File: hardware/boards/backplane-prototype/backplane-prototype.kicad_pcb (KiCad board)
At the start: 4 copper layers, 151.8 x 30.8 mm, 93 parts, among them J1 SLOT_1, J10 SWD, J11 12V 3-WIRE FAN, J12 DS18B20 EXT SUPPLY, J2 XY308-2.54-3P / EXTERNAL CAN, J3 SLOT_2, J4 SLOT_3, J5 DC IN, J6 SLOT_4, J7 SLOT_5, J8 SLOT_6, J9 12V 3-WIRE FAN, Q1 AO3407A, Q2 2N7002, Q3 AO3407A, Q4 2N7002, U1 STM32C092GCU6, U2 LM5164DDAR, U3 LM5164DDAR, U4 INA237AIDGSR, U5 TCAN3413DR

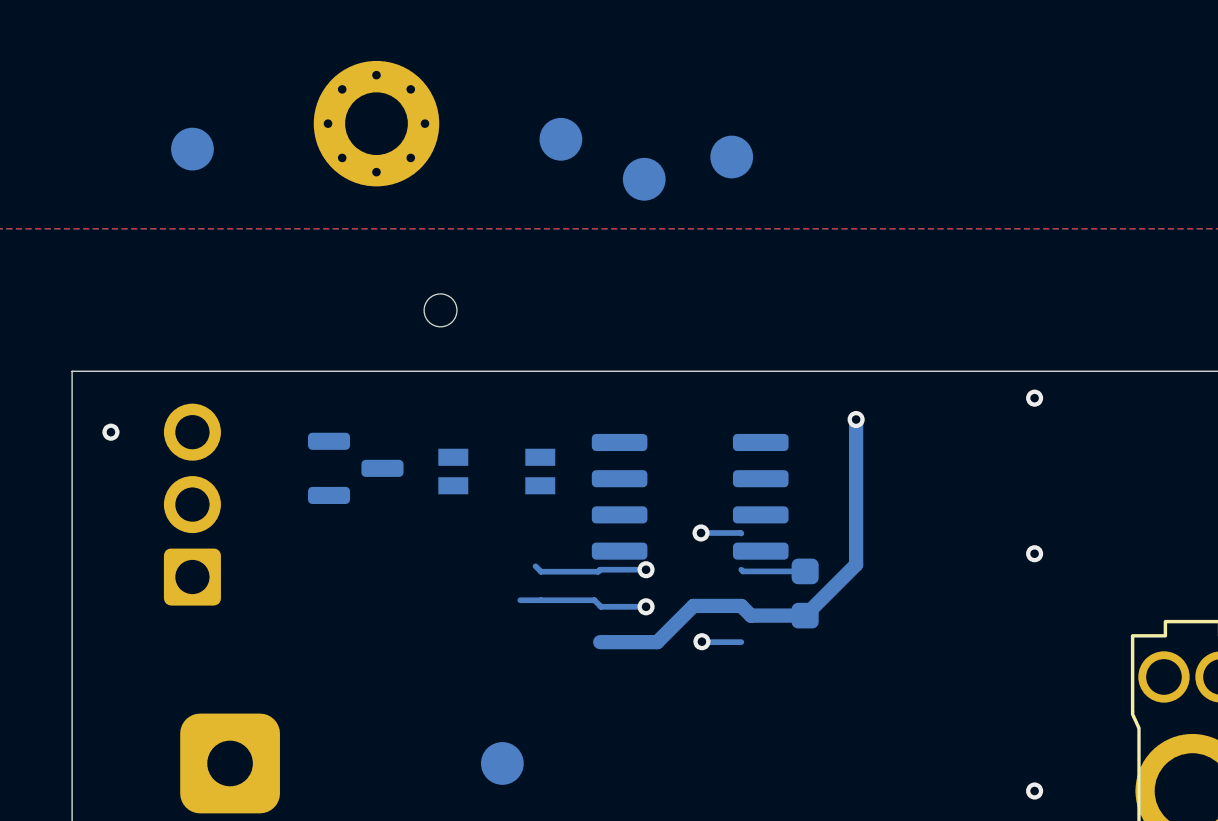
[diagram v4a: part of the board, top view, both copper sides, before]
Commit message: checkpoint: save CAN schematic and layout updates
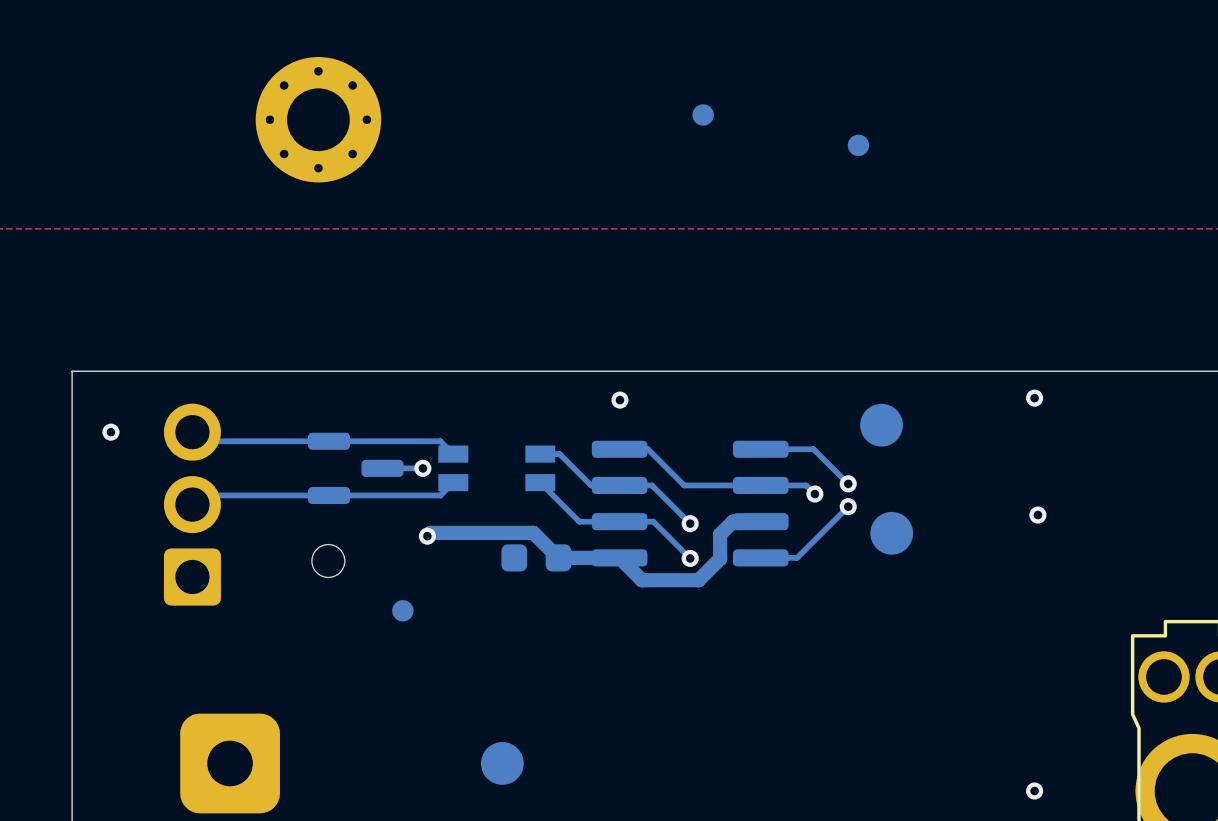
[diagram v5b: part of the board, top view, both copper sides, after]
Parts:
- removed TP15: CAN_BUS_P, TestPoint:TestPoint_Pad_D1.5mm
- removed TP16: CAN_BUS_N, TestPoint:TestPoint_Pad_D1.5mm
- added REF**: Fiducial_0.75mm_Mask1.5mm, Fiducial:Fiducial_0.75mm_Mask1.5mm, B.Cu at (41.1, 55.1)
- added REF**: Fiducial_0.75mm_Mask1.5mm, Fiducial:Fiducial_0.75mm_Mask1.5mm, B.Cu at (51.6, 37.7)
- added REF**: Fiducial_0.75mm_Mask1.5mm, Fiducial:Fiducial_0.75mm_Mask1.5mm, B.Cu at (57.1, 38.8)
- moved TP7 15.1 mm to (58.2, 52.4)
- moved TP6 10.8 mm to (57.9, 48.6)
- moved H9 9.63 mm to (38.5, 53.4)
- moved C20 9.51 mm to (45.8, 53.2), turned to 180 degrees
- moved H1 2.04 mm to (38.1, 37.9)
- moved U5 0.24 mm to (51.2, 51.3)
- moved L3 0.11 mm to (44.4, 50.1)
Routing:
- net /CAN-FD and Six Slots/CAN_EXT_N: track 0.00 -> 9.47 mm
- net /CAN-FD and Six Slots/CAN_EXT_P: track 0.13 -> 9.60 mm
- net GND: track 41.0 -> 47.6 mm, vias 58 -> 61
- net CAN_RX: track 106.3 -> 99.9 mm
- net CAN_TX: track 103.4 -> 99.7 mm
- net +3V3: track 274.8 -> 273.1 mm
- net /CAN-FD and Six Slots/CAN_BUS_P: track 140.1 -> 139.3 mm

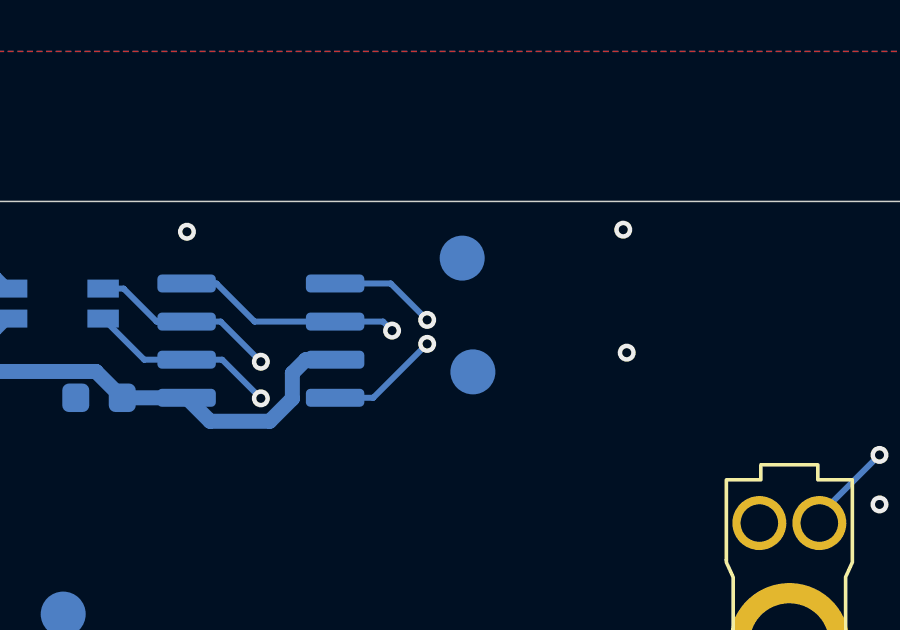
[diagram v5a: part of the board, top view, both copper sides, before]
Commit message: Move CAN test points beside signal vias
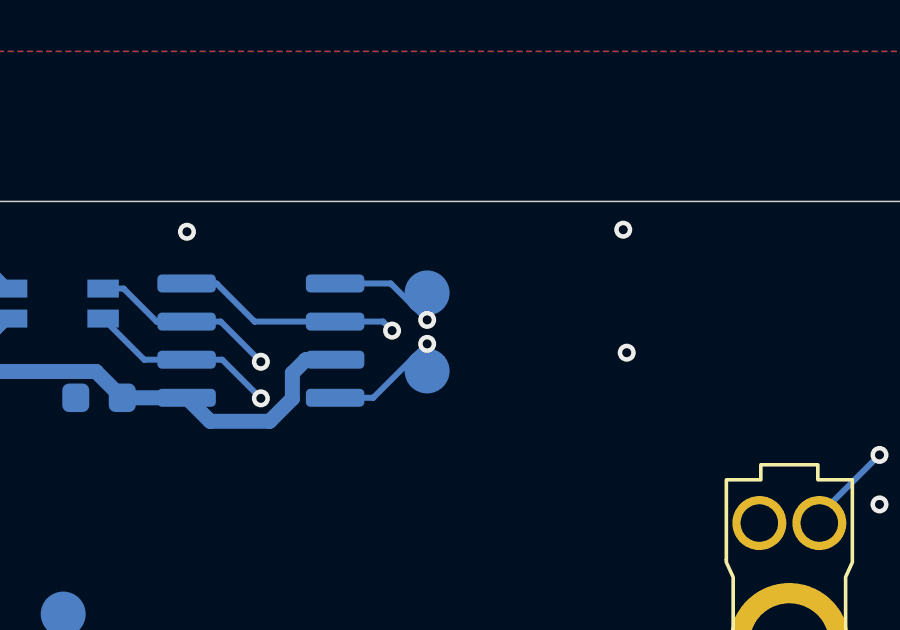
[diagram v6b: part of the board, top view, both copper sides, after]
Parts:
- moved TP6 1.65 mm to (56.7, 49.8)
- moved TP7 1.53 mm to (56.7, 52.4)
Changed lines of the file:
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@@
 	(footprint "TestPoint:TestPoint_Pad_D1.5mm"
 		(layer "B.Cu")
-		(at 57.889587 48.589479 180)
+		(at 56.72 49.75 180)
 		(descr "SMD pad as test Point, diameter 1.5mm")
 		(tags "test point SMD pad")
 		(property "Reference" "TP6"
-			(at 0 1.648 0)
+			(at -1.75 0 90)
 			(layer "B.SilkS")
 			(effects
@@
 			(end 0 -0.95)
 			(stroke
-				(width 0.12)
+				(width 0.15)
 				(type solid)
 			)
@@
 	(footprint "TestPoint:TestPoint_Pad_D1.5mm"
 		(layer "B.Cu")
-		(at 58.246097 52.381446 180)
+		(at 56.72 52.35 180)
 		(descr "SMD pad as test Point, diameter 1.5mm")
 		(tags "test point SMD pad")
 		(property "Reference" "TP7"
-			(at 0 1.648 0)
+			(at -3.28 0 90)
 			(layer "B.SilkS")
 			(effects
@@
 			(end 0 -0.95)
 			(stroke
-				(width 0.12)
-				(type solid)
-			)
+				(width 0.15)
+				(type solid)
+			)

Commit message: checkpoint: save current backplane layout
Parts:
- moved H9 14.7 mm to (50.5, 44.9)
- moved C20 14.7 mm to (57.8, 44.8)
- moved D1 14.7 mm to (51.4, 41.7)
- moved L3 14.7 mm to (56.4, 41.7)
- moved TP6 14.7 mm to (68.7, 41.3)
- moved TP7 14.7 mm to (68.7, 43.9)
- moved U5 14.7 mm to (63.2, 42.9)
- moved REF** 13.2 mm to (39.6, 42.0)
- moved H1 12.3 mm to (39.9, 50.1)
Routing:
- net /CAN-FD and Six Slots/CAN_EXT_N: track 9.47 -> 5.00 mm
- net /CAN-FD and Six Slots/CAN_EXT_P: track 9.60 -> 5.13 mm
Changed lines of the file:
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@@
 	(footprint "mini-rack-power:MountingHole_2.2mm_M2_Pad_Via_JLC"
 		(layer "F.Cu")
-		(at 38.138968 37.877687)
+		(at 39.863604 50.091978)
 		(descr "Mounting Hole 2.2mm, M2, with 0.3 mm stitching drills, 0.26 mm annular rings, and 0.45 mm hole clearance")
 		(tags "mountinghole M2 JLCPCB")
@@
 	(footprint "Capacitor_SMD:C_0603_1608Metric"
 		(layer "B.Cu")
-		(at 45.783704 53.245 180)
+		(at 57.775494 44.819757 180)
 		(descr "Capacitor SMD 0603 (1608 Metric), square (rectangular) end terminal, IPC-7351 nominal, (Body size source: IPC-SM-782 page 76, https://www.pcb-3d.com/wordpress/wp-content/uploads/ipc-sm-782a_amendment_1_and_2.pdf)")
 		(tags "capacitor")
@@
 	(footprint "Fiducial:Fiducial_0.75mm_Mask1.5mm"
 		(layer "B.Cu")
-		(at 41.101509 55.100021 180)
+		(at 39.641394 41.981327 180)
 		(descr "Fiducial, circular marking, 0.75mm bare copper, 1.5mm soldermask opening (Level B)")
 		(tags "fiducial")
@@
 	(footprint "TestPoint:TestPoint_Pad_D1.5mm"
 		(layer "B.Cu")
-		(at 56.72 49.75 180)
+		(at 68.71179 41.324757 180)
 		(descr "SMD pad as test Point, diameter 1.5mm")
 		(tags "test point SMD pad")
@@
 	(footprint "TestPoint:TestPoint_Pad_D1.5mm"
 		(layer "B.Cu")
-		(at 56.72 52.35 180)
+		(at 68.71179 43.924757 180)
 		(descr "SMD pad as test Point, diameter 1.5mm")
 		(tags "test point SMD pad")
@@
 	(footprint "mini-rack-power:MountingHole_JLCPCB_Tooling_1.152mm"
 		(layer "B.Cu")
-		(at 38.486819 53.353745 180)
+		(at 50.478609 44.928502 180)
 		(descr "JLCPCB PCBA tooling hole: 1.152 mm round NPTH with 0.148 mm solder-mask expansion")
 		(tags "mountinghole tooling JLCPCB PCBA NPTH 1.152mm")
@@
 	(footprint "Package_SO:SOIC-8_3.9x4.9mm_P1.27mm"
 		(layer "B.Cu")
-		(at 51.17833 51.34 180)
+		(at 63.17012 42.914757 180)
 		(descr "SOIC, 8 Pin (JEDEC MS-012AA, https://www.analog.com/media/en/package-pcb-resources/package/pkg_pdf/soic_narrow-r/r_8.pdf)")
 		(tags "SOIC SO")
@@
 	)
 	(footprint "mini-rack-power:L_CommonModeChoke_TDK_ACT1210D"
-		(locked yes)
 		(layer "B.Cu")
-		(at 44.394686 50.105 180)
+		(at 56.386476 41.679757 180)
 		(descr "TDK ACT1210D automotive CAN/CAN-FD common-mode choke, 3.2 x 2.5 mm body; manufacturer recommended 4.1 x 1.6 mm land pattern")
 		(tags "common mode choke CAN CAN-FD TDK ACT1210D C3039743")
@@
 	)
 	(footprint "Package_TO_SOT_SMD:SOT-23"
-		(locked yes)
 		(layer "B.Cu")
-		(at 39.447877 50.105)
+		(at 51.439667 41.679757)
 		(descr "SOT, 3 Pin (JEDEC TO-236 Var AB https://www.jedec.org/document_search?search_api_views_fulltext=TO-236)")
 		(tags "SOT TO_SOT_SMD")
@@
 	)
 	(footprint "mini-rack-power:TerminalBlock_Xinya_XY308-2.54-3P_1x03_P2.54mm_Horizontal"
+		(locked yes)
 		(layer "B.Cu")
 		(at 33.72 53.915 90)
@@
 	)
 	(via
-		(at 48.715082 47.710566)
+		(at 60.706872 39.285323)
 		(size 0.6)
 		(drill 0.3)
@@
 	)
 	(via
-		(at 55.552012 51.005603)
+		(at 67.543802 42.58036)
 		(size 0.6)
 		(drill 0.3)
@@
 	)
 	(via
-		(at 41.803281 50.105)
+		(at 53.795071 41.679757)
 		(size 0.6)
 		(drill 0.3)
@@
 	)
 	(segment
-		(start 50.969756 50.705)
-		(end 49.699756 49.435)
+		(start 62.961546 42.279757)
+		(end 61.691546 41.009757)
 		(width 0.2)
 		(layer "B.Cu")
@@
 	)
 	(segment
-		(start 53.65333 50.705)
-		(end 50.969756 50.705)
+		(start 65.64512 42.279757)
+		(end 62.961546 42.279757)
 		(width 0.2)
 		(layer "B.Cu")
@@
 	)
 	(segment
-		(start 49.699756 49.435)
-		(end 48.70333 49.435)
+		(start 61.691546 41.009757)
+		(end 60.69512 41.009757)
 		(width 0.2)
 		(layer "B.Cu")
@@
 	)
 	(segment
-		(start 55.552012 51.005603)
-		(end 55.251409 50.705)
+		(start 67.543802 42.58036)
+		(end 67.243199 42.279757)
 		(width 0.2)
 		(layer "B.Cu")
@@
 	)
 	(segment
-		(start 41.803281 50.105)
-		(end 40.385377 50.105)
+		(start 53.795071 41.679757)
+		(end 52.377167 41.679757)
 		(width 0.2)
 		(layer "B.Cu")
@@
 	)
 	(segment
-		(start 55.251409 50.705)
-		(end 53.65333 50.705)
+		(start 67.243199 42.279757)
+		(end 65.64512 42.279757)
 		(width 0.2)
 		(layer "B.Cu")
@@
 	)
 	(via
-		(at 51.17833 52.043935)
+		(at 63.17012 43.618692)
 		(size 0.6)
 		(drill 0.3)
 		(layers "F.Cu" "B.Cu")
-		(locked yes)
 		(net "/CAN-FD and Six Slots/CAN_BUS_P")
 	)
@@
 	)
 	(segment
-		(start 48.70333 50.705)
-		(end 47.70333 50.705)
+		(start 60.69512 42.279757)
+		(end 59.69512 42.279757)
 		(width 0.2)
 		(layer "B.Cu")
@@
 	)
 	(segment
-		(start 47.70333 50.705)
-		(end 46.60333 49.605)
+		(start 59.69512 42.279757)
+		(end 58.59512 41.179757)
 		(width 0.2)
 		(layer "B.Cu")
@@
 	)
 	(segment
-		(start 51.17833 52.043935)
-		(end 49.839395 50.705)
+		(start 63.17012 43.618692)
+		(end 61.831185 42.279757)
 		(width 0.2)
 		(layer "B.Cu")
@@
 	)
 	(segment
-		(start 49.839395 50.705)
-		(end 48.70333 50.705)
+		(start 61.831185 42.279757)
+		(end 60.69512 42.279757)
 		(width 0.2)
 		(layer "B.Cu")
@@
 	)
 	(segment
-		(start 46.60333 49.605)
-		(end 45.919686 49.605)
+		(start 58.59512 41.179757)
+		(end 57.911476 41.179757)
 		(width 0.2)
 		(layer "B.Cu")
@@
 	)
 	(via
-		(at 51.17833 53.263576)
+		(at 63.17012 44.838333)
 		(size 0.6)
 		(drill 0.3)
 		(layers "F.Cu" "B.Cu")
-		(locked yes)
 		(net "/CAN-FD and Six Slots/CAN_BUS_N")
 	)
@@
 	)
 	(segment
-		(start 47.289686 51.975)
-		(end 45.919686 50.605)
+		(start 59.281476 43.549757)
+		(end 57.911476 42.179757)
 		(width 0.2)
 		(layer "B.Cu")
@@
 	)
 	(segment
-		(start 48.70333 51.975)
-		(end 47.289686 51.975)
+		(start 60.69512 43.549757)
+		(end 59.281476 43.549757)
 		(width 0.2)
 		(layer "B.Cu")
@@
 	)
 	(segment
-		(start 51.17833 53.263576)
-		(end 49.889754 51.975)
+		(start 63.17012 44.838333)
+		(end 61.881544 43.549757)
 		(width 0.2)
 		(layer "B.Cu")
@@
 	)
 	(segment
-		(start 49.889754 51.975)
-		(end 48.70333 51.975)
+		(start 61.881544 43.549757)
+		(end 60.69512 43.549757)
 		(width 0.2)
 		(layer "B.Cu")
@@
 	)
 	(via
-		(at 41.961545 52.482437)
+		(at 53.953335 44.057194)
 		(size 0.6)
 		(drill 0.3)
@@
 	)
 	(segment
-		(start 51.474633 54.027934)
-		(end 52.22833 53.274237)
+		(start 63.466423 45.602691)
+		(end 64.22012 44.848994)
 		(width 0.5)
 		(layer "B.Cu")
@@
 	)
 	(segment
-		(start 52.22833 52.425001)
-		(end 52.678331 51.975)
+		(start 64.22012 43.999758)
+		(end 64.670121 43.549757)
 		(width 0.5)
 		(layer "B.Cu")
@@
 	)
 	(segment
-		(start 41.961545 52.482437)
-		(end 42.076038 52.367944)
+		(start 53.953335 44.057194)
+		(end 54.067828 43.942701)
 		(width 0.5)
 		(layer "B.Cu")
@@
 	)
 	(segment
-		(start 49.486264 54.027934)
-		(end 48.70333 53.245)
+		(start 61.478054 45.602691)
+		(end 60.69512 44.819757)
 		(width 0.5)
 		(layer "B.Cu")
@@
 	)
 	(segment
-		(start 51.474633 54.027934)
-		(end 49.486264 54.027934)
+		(start 63.466423 45.602691)
+		(end 61.478054 45.602691)
 		(width 0.5)
 		(layer "B.Cu")
@@
 	)
 	(segment
-		(start 42.076038 52.367944)
-		(end 45.681648 52.367944)
+		(start 54.067828 43.942701)
+		(end 57.673438 43.942701)
 		(width 0.5)
 		(layer "B.Cu")
@@
 	)
 	(segment
-		(start 52.678331 51.975)
-		(end 53.65333 51.975)
+		(start 64.670121 43.549757)
+		(end 65.64512 43.549757)
 		(width 0.5)
 		(layer "B.Cu")
@@
 	)
 	(segment
-		(start 45.681648 52.367944)
-		(end 46.558704 53.245)
+		(start 57.673438 43.942701)
+		(end 58.550494 44.819757)
 		(width 0.5)
 		(layer "B.Cu")
@@
 	)
 	(segment
-		(start 46.558704 53.245)
-		(end 48.70333 53.245)
+		(start 58.550494 44.819757)
+		(end 60.69512 44.819757)
 		(width 0.5)
 		(layer "B.Cu")
@@
 	)
 	(segment
-		(start 52.22833 53.274237)
-		(end 52.22833 52.425001)
+		(start 64.22012 44.848994)
+		(end 64.22012 43.999758)
 		(width 0.5)
 		(layer "B.Cu")
@@
 	)
 	(via
-		(at 56.72163 50.648745)
+		(at 68.71342 42.223502)
 		(size 0.6)
 		(drill 0.3)
 		(layers "F.Cu" "B.Cu")
-		(locked yes)
 		(free yes)
 		(net "CAN_TX")
@@
 	)
 	(segment
-		(start 55.507885 49.435)
-		(end 53.65333 49.435)
+		(start 67.499675 41.009757)
+		(end 65.64512 41.009757)
 		(width 0.2)
 		(layer "B.Cu")
@@
 	)
 	(segment
-		(start 56.72163 50.648745)
-		(end 55.507885 49.435)
+		(start 68.71342 42.223502)
+		(end 67.499675 41.009757)
 		(width 0.2)
 		(layer "B.Cu")
@@
 	)
 	(via
-		(at 56.72163 51.448028)
+		(at 68.71342 43.022785)
 		(size 0.6)
 		(drill 0.3)
 		(layers "F.Cu" "B.Cu")
-		(locked yes)
 		(free yes)
 		(net "CAN_RX")
@@
 	)
 	(segment
-		(start 56.72163 51.448028)
-		(end 54.924658 53.245)
+		(start 68.71342 43.022785)
+		(end 66.916448 44.819757)
 		(width 0.2)
 		(layer "B.Cu")
@@
 	)
 	(segment
-		(start 54.924658 53.245)
-		(end 53.65333 53.245)
+		(start 66.916448 44.819757)
+		(end 65.64512 44.819757)
 		(width 0.2)
 		(layer "B.Cu")
@@
 	)
 	(segment
-		(start 42.869686 50.605)
-		(end 42.419686 51.055)
-		(width 0.2)
-		(layer "B.Cu")
-		(net "/CAN-FD and Six Slots/CAN_EXT_N")
-	)
-	(segment
-		(start 38.510377 51.055)
-		(end 34.04 51.055)
+		(start 54.861476 42.179757)
+		(end 54.411476 42.629757)
 		(width 0.2)
 		(layer "B.Cu")
@@
 	)
 	(segment
-		(start 42.419686 51.055)
-		(end 38.510377 51.055)
+		(start 54.411476 42.629757)
+		(end 50.502167 42.629757)
 		(width 0.2)
 		(layer "B.Cu")
@@
 	)
 	(segment
-		(start 38.510377 49.155)
-		(end 42.419686 49.155)
+		(start 50.502167 40.729757)
+		(end 54.411476 40.729757)
 		(width 0.2)
 		(layer "B.Cu")
@@
 	)
 	(segment
-		(start 42.419686 49.155)
-		(end 42.869686 49.605)
+		(start 54.411476 40.729757)
+		(end 54.861476 41.179757)
 		(width 0.2)
 		(layer "B.Cu")
@@
 		(width 0.2)
 		(layer "B.Cu")
-		(net "/CAN-FD and Six Slots/CAN_EXT_P")
-	)
-	(segment
-		(start 38.510377 49.155)
-		(end 34.04 49.155)
-		(width 0.2)
-		(layer "B.Cu")

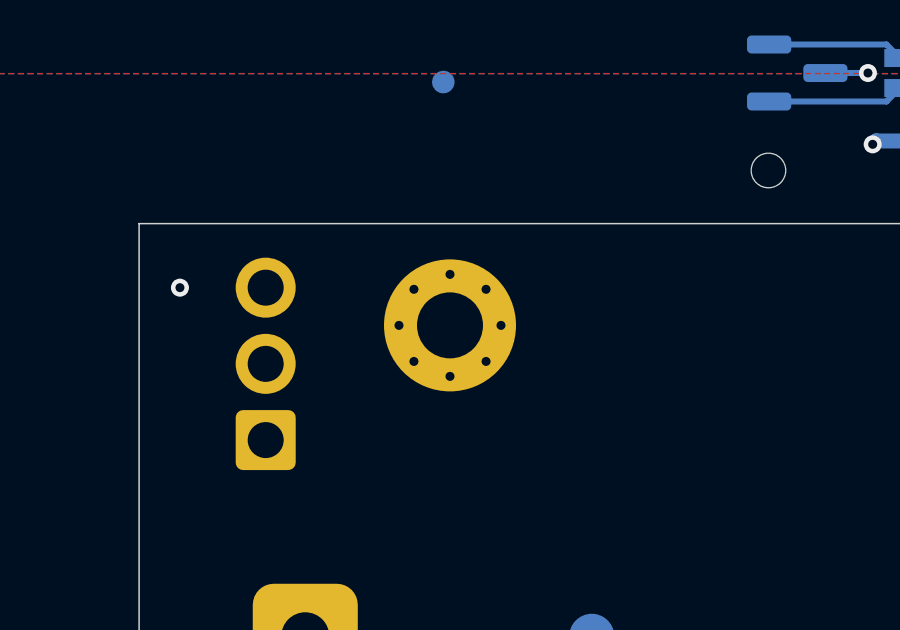
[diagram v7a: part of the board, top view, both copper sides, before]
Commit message: Move H1 toward upper-left corner
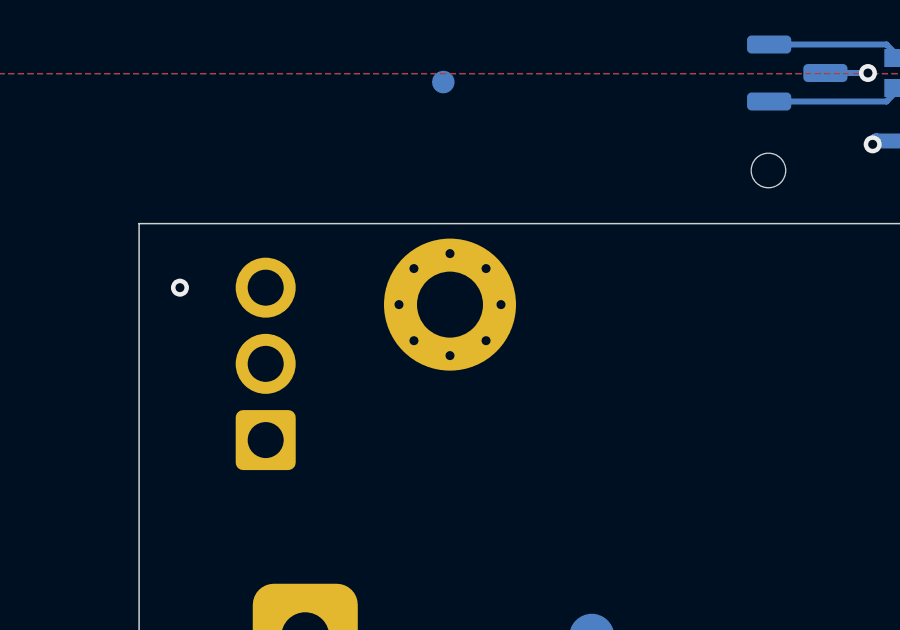
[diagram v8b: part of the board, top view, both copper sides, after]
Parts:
- moved H1 0.69 mm to (39.9, 49.4)
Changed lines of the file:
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@@
 	(footprint "mini-rack-power:MountingHole_2.2mm_M2_Pad_Via_JLC"
 		(layer "F.Cu")
-		(at 39.863604 50.091978)
+		(at 39.863604 49.4)
 		(descr "Mounting Hole 2.2mm, M2, with 0.3 mm stitching drills, 0.26 mm annular rings, and 0.45 mm hole clearance")
 		(tags "mountinghole M2 JLCPCB")
